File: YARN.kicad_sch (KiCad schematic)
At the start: 10 parts, among them J1 Cart System Out, J2 Cart Main In, J3 Cart Sub In, SW1 SW_SPDT, U1 74HC244, U2 74HC244

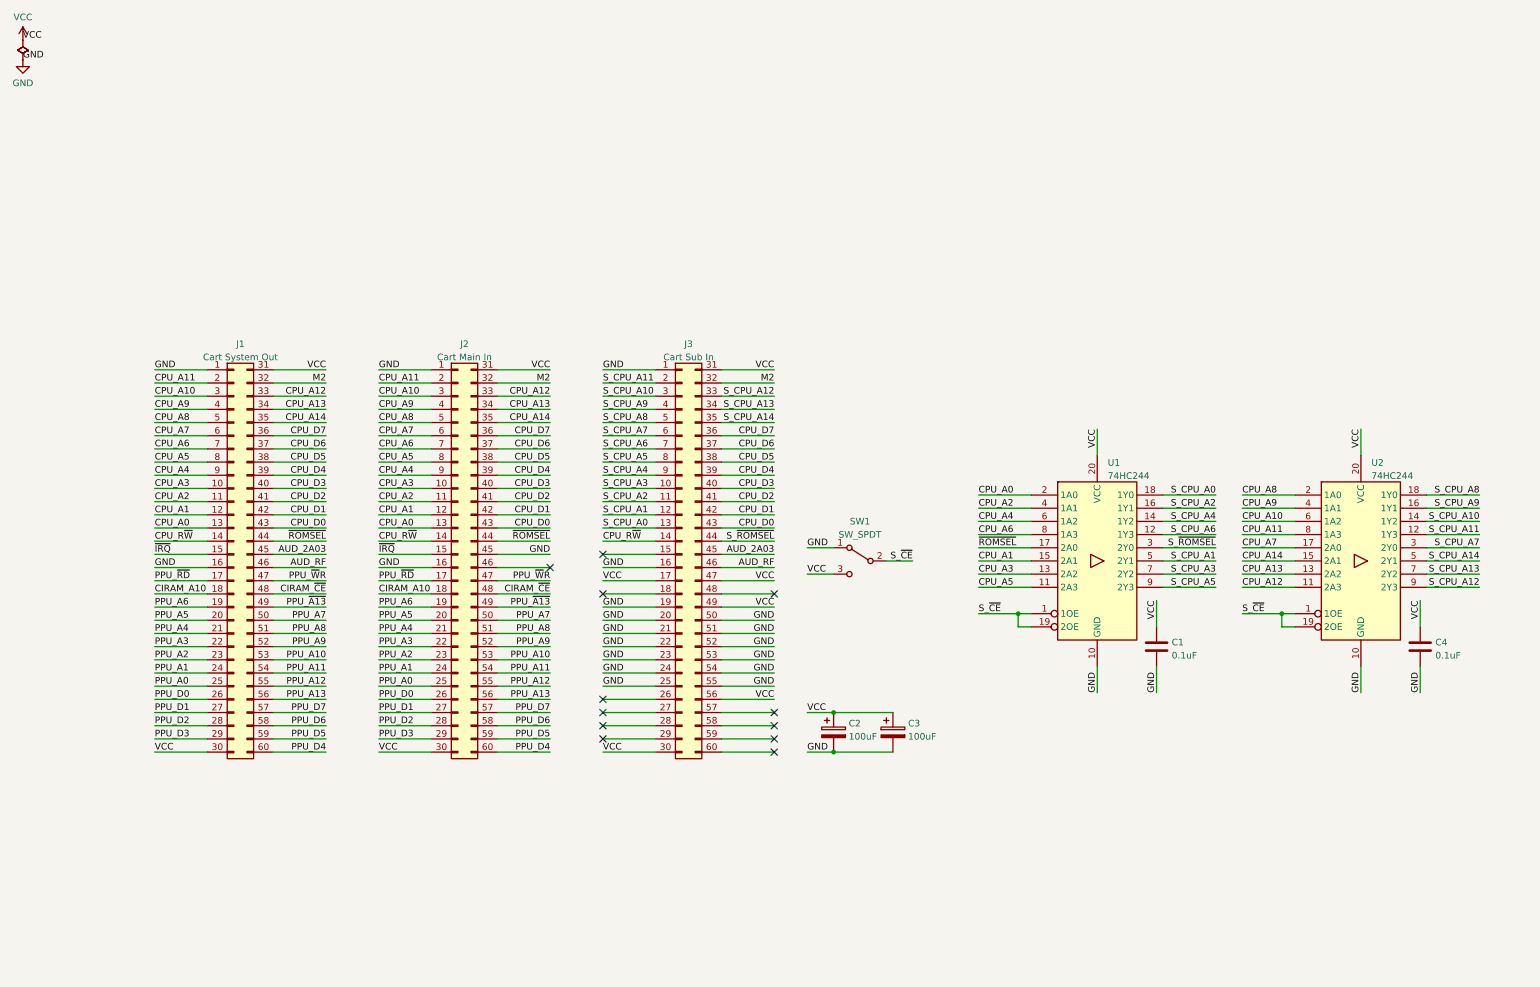
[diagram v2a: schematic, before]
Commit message: Buffer data and addr bus, add switch for VRC6 A/B
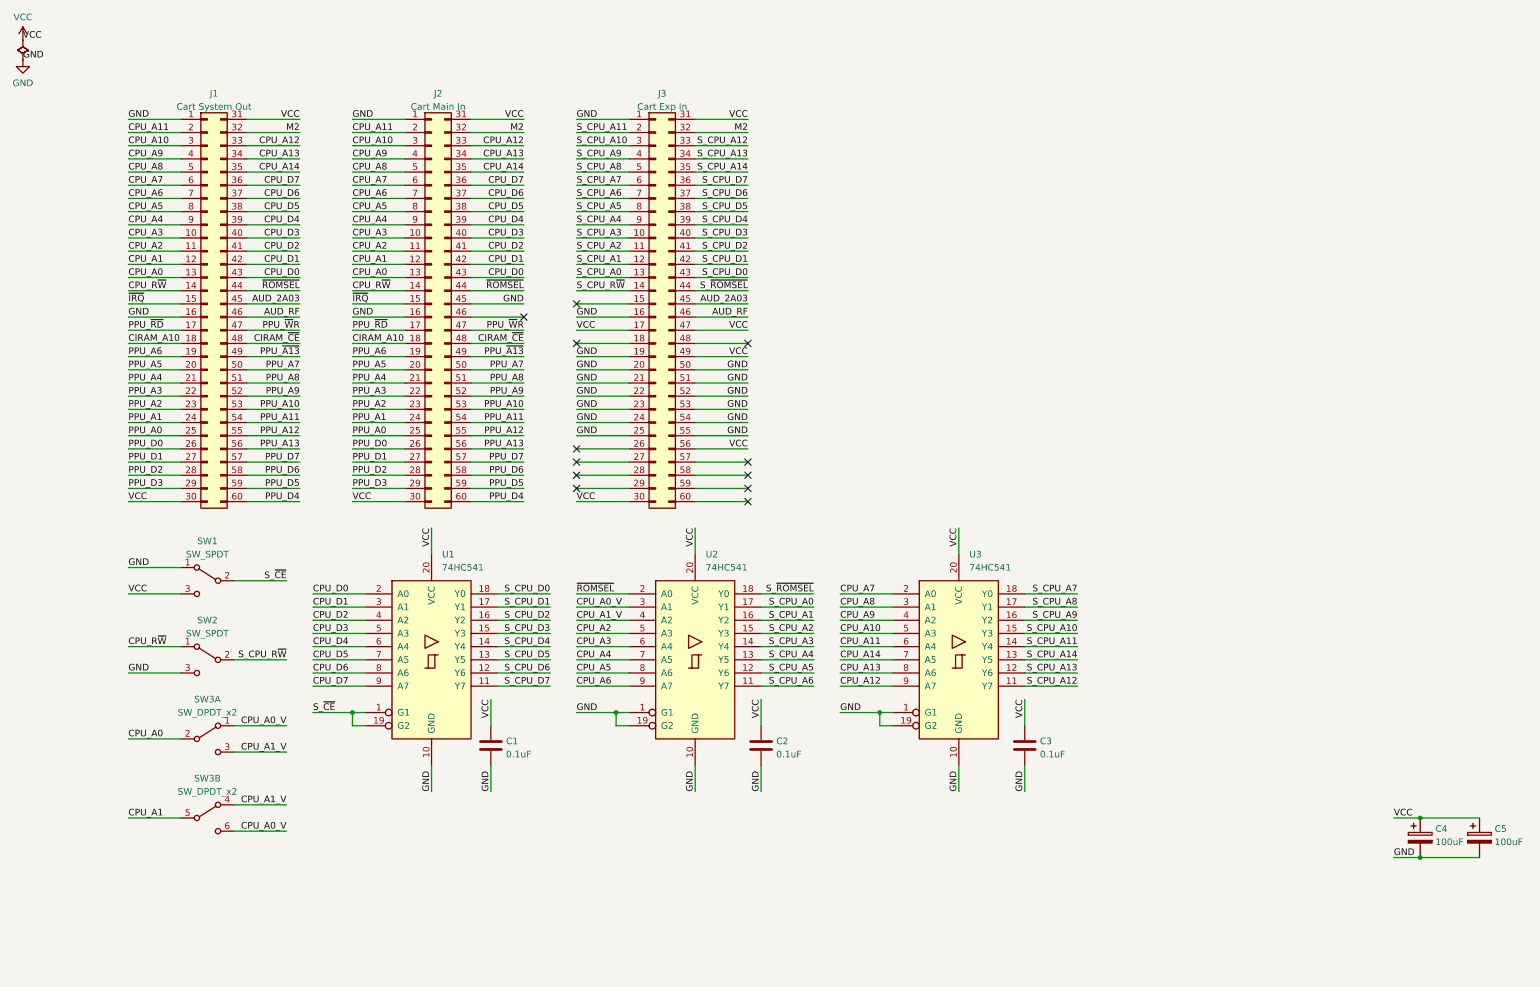
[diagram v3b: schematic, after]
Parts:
- removed C4: 0.1uF, YARN:C_Disc-0805_D3.0mm_W1.6mm_P2.50mm, symbol Device:C
- removed U1, U2: 74HC244, Package_SO:SOIC-20W_7.5x12.8mm_P1.27mm, symbol 74xx:74HC244
- added C2, C3: 0.1uF, YARN:C_Disc-0805_D3.0mm_W1.6mm_P2.50mm, symbol Device:C
- added SW2: SW_SPDT, YARN:SK-3390A-L0, symbol Switch:SW_SPDT
- added SW3: SW_DPDT_x2, YARN:SS-3390S-L0, symbol Switch:SW_DPDT_x2
- added U1, U2, U3: 74HC541, Package_SO:SOIC-20W_7.5x12.8mm_P1.27mm, symbol 74xx:74LS541
- C4: renamed from C2; footprint Capacitor_THT:CP_Radial_D5.0mm_P2.50mm -> Capacitor_SMD:CP_Elec_6.3x5.4
- C5: renamed from C3; footprint Capacitor_THT:CP_Radial_D5.0mm_P2.50mm -> Capacitor_SMD:CP_Elec_6.3x5.4
- J3: value Cart Sub In -> Cart Exp In
- SW1: footprint YARN:JS102011SCQN -> YARN:SK-3390A-L0
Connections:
- net CPU_A0: now also SW3.2 (B)
- net CPU_A1: now also SW3.5 (B)
- net CPU_A10: now also U3.5 (A3)
- net CPU_A11: now also U3.6 (A4)
- net CPU_A12: now also U3.9 (A7)
- net CPU_A13: now also U3.8 (A6)
- net CPU_A14: now also U3.7 (A5)
- net CPU_A2: now also U2.5 (A3)
- net CPU_A3: now also U2.6 (A4)
- net CPU_A4: now also U2.7 (A5)
- net CPU_A5: now also U2.8 (A6)
- net CPU_A6: now also U2.9 (A7)
- net CPU_A7: now also U3.2 (A0)
- net CPU_A8: now also U3.3 (A1)
- net CPU_A9: now also U3.4 (A2)
- net CPU_D0: now also U1.2 (A0); no longer J3.43 (Pin_43)
- net CPU_D1: now also U1.3 (A1); no longer J3.42 (Pin_42)
- net CPU_D2: now also U1.4 (A2); no longer J3.41 (Pin_41)
- net CPU_D3: now also U1.5 (A3); no longer J3.40 (Pin_40)
- net CPU_D4: now also U1.6 (A4); no longer J3.39 (Pin_39)
- net CPU_D5: now also U1.7 (A5); no longer J3.38 (Pin_38)
- net CPU_D6: now also U1.8 (A6); no longer J3.37 (Pin_37)
- net CPU_D7: now also U1.9 (A7); no longer J3.36 (Pin_36)
- net CPU_R~{W}: now also SW2.1 (A); no longer J3.14 (Pin_14)
- net GND: now also C2.2, C3.2, SW2.3 (C), U1.10 (GND), U2.1 (G1), U2.10 (GND), U2.19 (G2), U3.1 (G1), U3.10 (GND), U3.19 (G2)
- net S_CPU_A0: now also U2.17 (Y1)
- net S_CPU_A1: now also U2.16 (Y2)
- net S_CPU_A10: now also U3.15 (Y3)
- net S_CPU_A11: now also U3.14 (Y4)
- net S_CPU_A12: now also U3.11 (Y7)
- net S_CPU_A13: now also U3.12 (Y6)
- net S_CPU_A14: now also U3.13 (Y5)
- net S_CPU_A2: now also U2.15 (Y3)
- net S_CPU_A3: now also U2.14 (Y4)
- net S_CPU_A4: now also U2.13 (Y5)
- net S_CPU_A5: now also U2.12 (Y6)
- net S_CPU_A6: now also U2.11 (Y7)
- net S_CPU_A7: now also U3.18 (Y0)
- net S_CPU_A8: now also U3.17 (Y1)
- net S_CPU_A9: now also U3.16 (Y2)
- net S_~{CE}: now also U1.1 (G1), U1.19 (G2)
- net S_~{ROMSEL}: now also U2.18 (Y0)
- net VCC: now also C2.1, C3.1, U1.20 (VCC), U2.20 (VCC), U3.20 (VCC)
- net ~{ROMSEL}: now also U2.2 (A0)
- new net CPU_A0_V: SW3.1 (A), SW3.6 (C), U2.3 (A1)
- new net CPU_A1_V: SW3.3 (C), SW3.4 (A), U2.4 (A2)
- new net S_CPU_D0: J3.43 (Pin_43), U1.18 (Y0)
- new net S_CPU_D1: J3.42 (Pin_42), U1.17 (Y1)
- new net S_CPU_D2: J3.41 (Pin_41), U1.16 (Y2)
- new net S_CPU_D3: J3.40 (Pin_40), U1.15 (Y3)
- new net S_CPU_D4: J3.39 (Pin_39), U1.14 (Y4)
- new net S_CPU_D5: J3.38 (Pin_38), U1.13 (Y5)
- new net S_CPU_D6: J3.37 (Pin_37), U1.12 (Y6)
- new net S_CPU_D7: J3.36 (Pin_36), U1.11 (Y7)
- new net S_CPU_R~{W}: J3.14 (Pin_14), SW2.2 (B)
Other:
- moved on the sheet: C1, C4, C5, J1, J2, J3, SW1

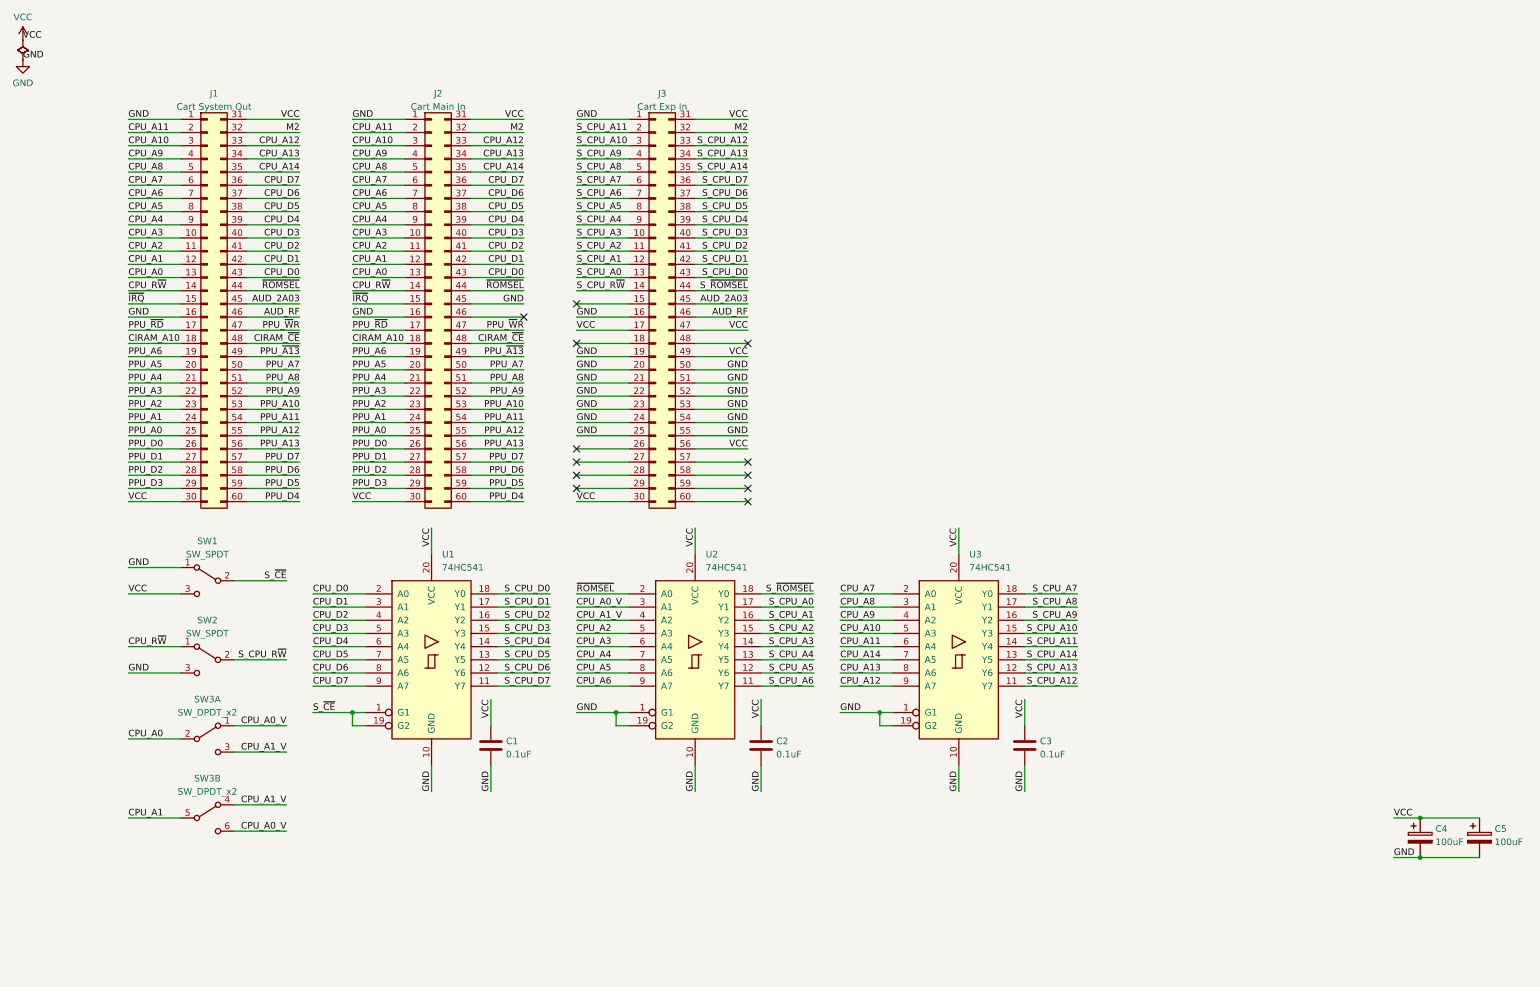
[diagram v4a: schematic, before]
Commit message: Redesign decoding architecture
Thanks, lidnariq and Perkka!
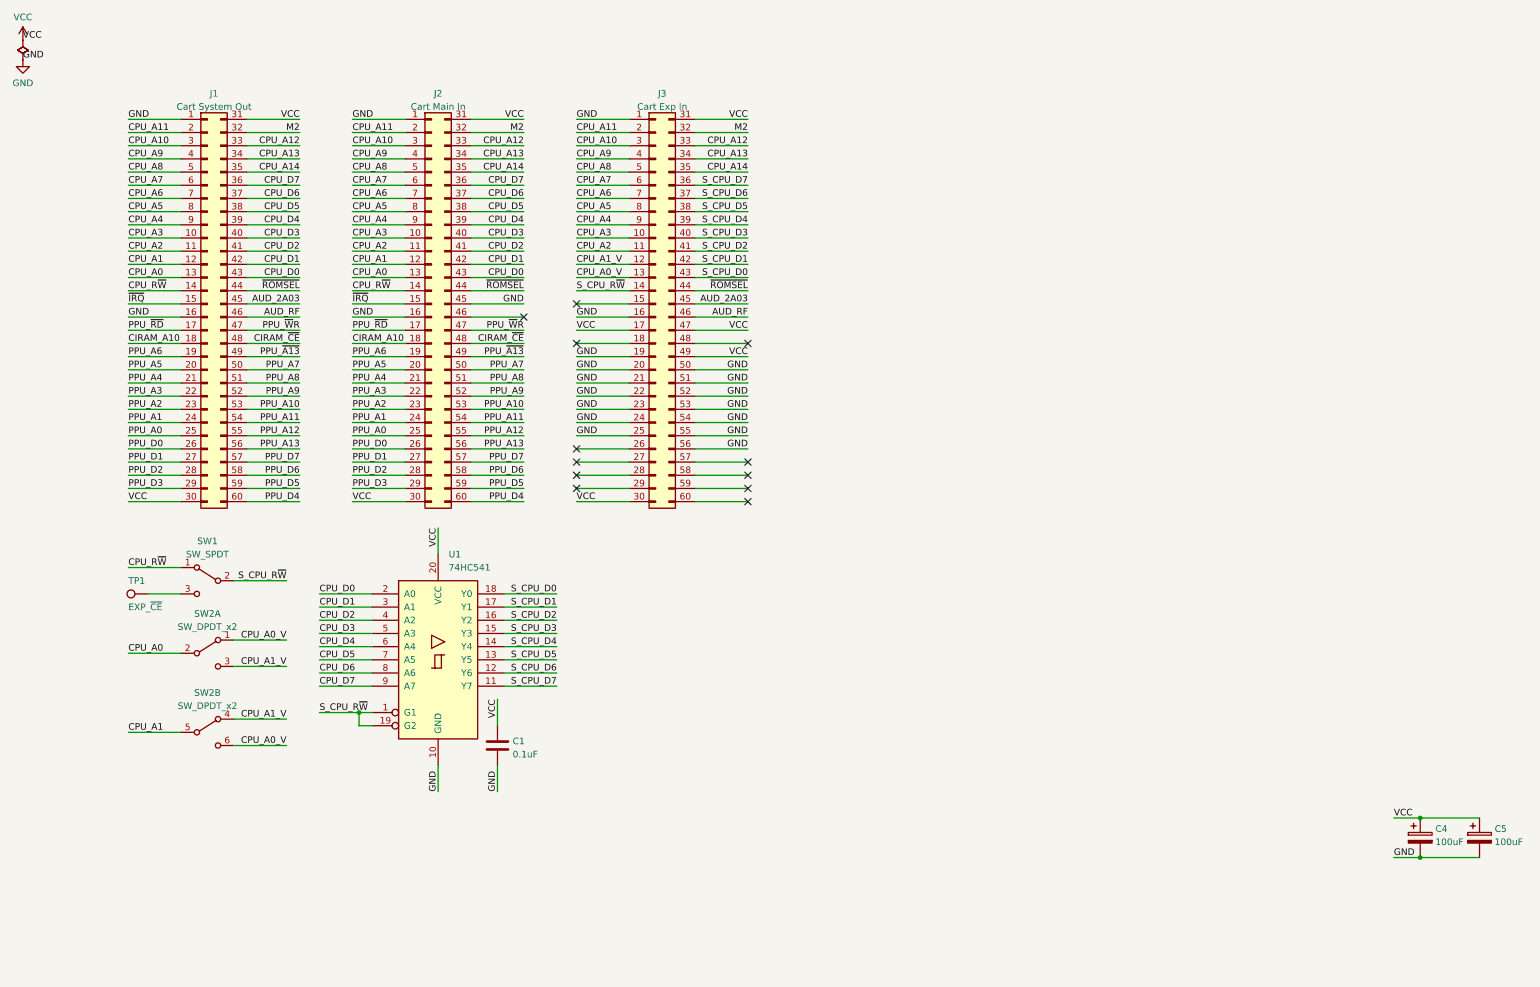
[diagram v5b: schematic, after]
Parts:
- removed C2, C3: 0.1uF, YARN:C_Disc-0805_D3.0mm_W1.6mm_P2.50mm, symbol Device:C
- removed SW2: SW_SPDT, YARN:SK-3390A-L0, symbol Switch:SW_SPDT
- removed U2, U3: 74HC541, Package_SO:SOIC-20W_7.5x12.8mm_P1.27mm, symbol 74xx:74LS541
- added TP1: EXP_~{CE}, TestPoint:TestPoint_Pad_D2.0mm, symbol Connector:TestPoint
- renumbered SW3 to SW2
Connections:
- net S_CPU_A0 is gone; now on net CPU_A0_V: J3.13 (Pin_13)
- net S_CPU_A1 is gone; now on net CPU_A1_V: J3.12 (Pin_12)
- net S_CPU_A10 is gone; now on net CPU_A10: J3.3 (Pin_3)
- net S_CPU_A11 is gone; now on net CPU_A11: J3.2 (Pin_2)
- net S_CPU_A12 is gone; now on net CPU_A12: J3.33 (Pin_33)
- net S_CPU_A13 is gone; now on net CPU_A13: J3.34 (Pin_34)
- net S_CPU_A14 is gone; now on net CPU_A14: J3.35 (Pin_35)
- net S_CPU_A2 is gone; now on net CPU_A2: J3.11 (Pin_11)
- net S_CPU_A3 is gone; now on net CPU_A3: J3.10 (Pin_10)
- net S_CPU_A4 is gone; now on net CPU_A4: J3.9 (Pin_9)
- net S_CPU_A5 is gone; now on net CPU_A5: J3.8 (Pin_8)
- net S_CPU_A6 is gone; now on net CPU_A6: J3.7 (Pin_7)
- net S_CPU_A7 is gone; now on net CPU_A7: J3.6 (Pin_6)
- net S_CPU_A8 is gone; now on net CPU_A8: J3.5 (Pin_5)
- net S_CPU_A9 is gone; now on net CPU_A9: J3.4 (Pin_4)
- net S_~{CE} is gone; now on net S_CPU_R~{W}: SW1.2 (B), U1.1 (G1), U1.19 (G2)
- net S_~{ROMSEL} is gone; now on net ~{ROMSEL}: J3.44 (Pin_44)
- net CPU_R~{W}: now also SW1.1 (A)
- net GND: now also J3.56 (Pin_56); no longer SW1.1 (A)
- net VCC: no longer J3.56 (Pin_56), SW1.3 (C)
- new net: SW1.3 (C), TP1.1
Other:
- moved on the sheet: C1, SW2A, SW2B, U1
